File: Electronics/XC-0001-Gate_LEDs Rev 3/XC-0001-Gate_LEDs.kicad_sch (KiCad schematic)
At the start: 21 parts, among them J1 DC12V_IN, J2 Driver_Ext, J3 LED_DIM, J4 LED_NODIM, J5 AC_IN, J6 AC_OUT, J7 Dim_Select, U1 LDU1416S1000

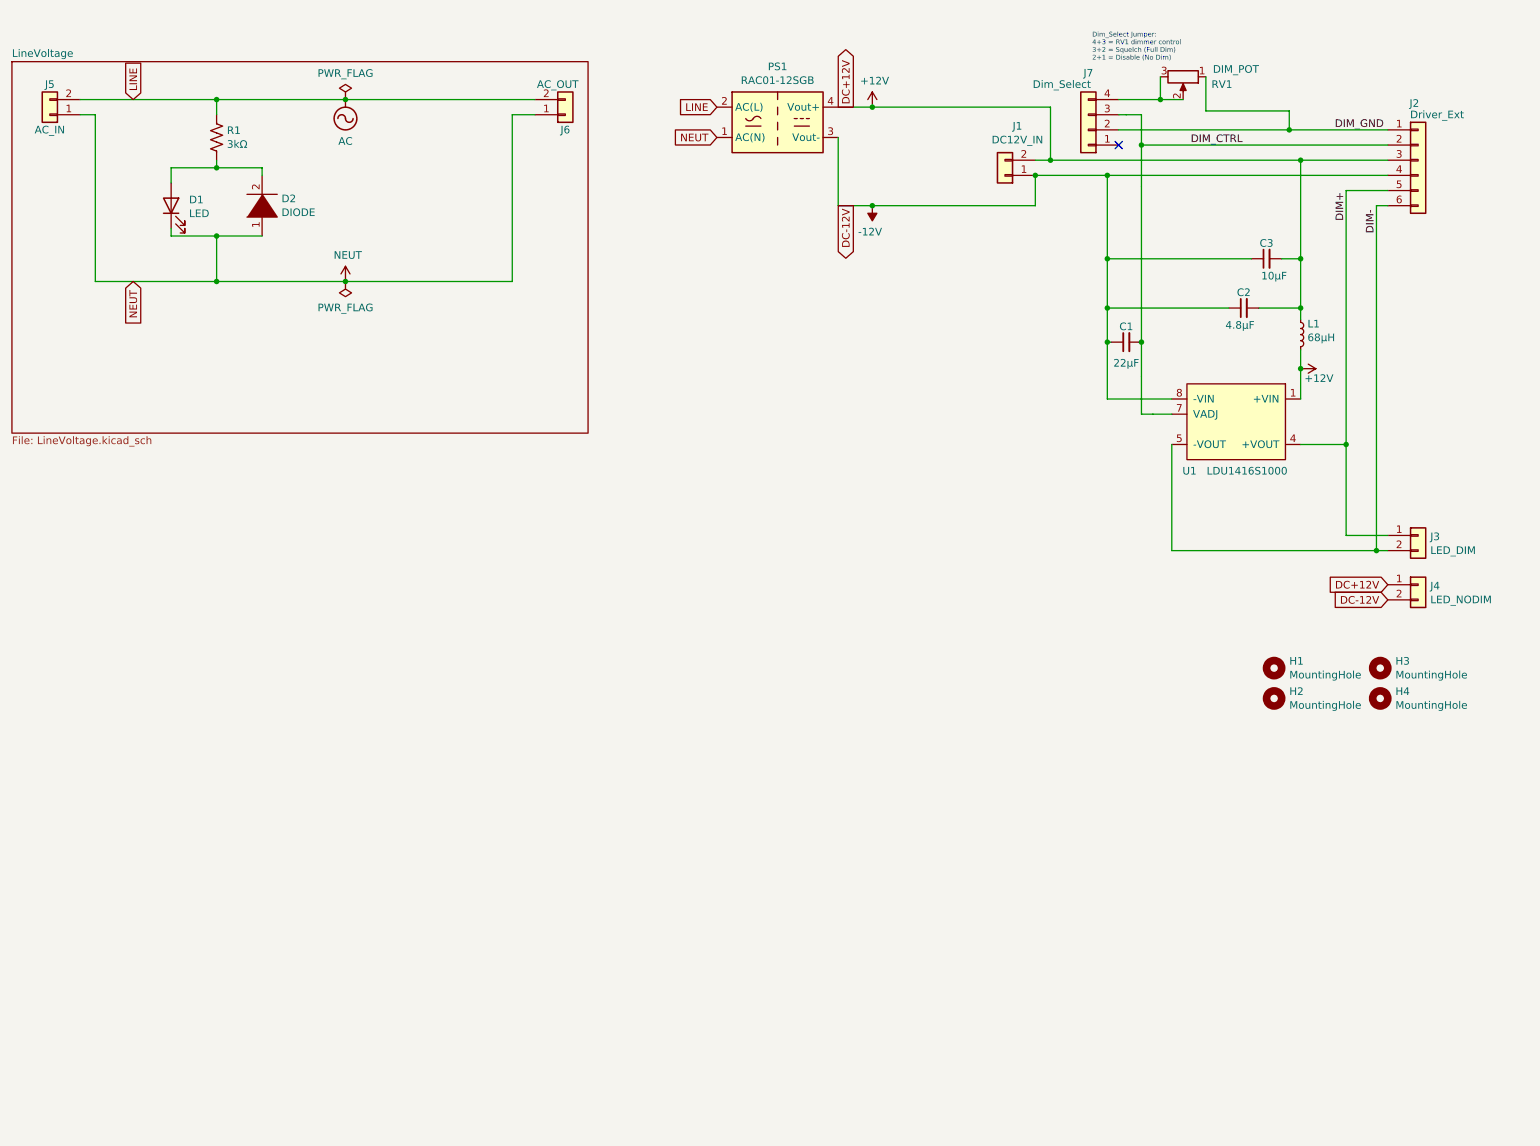
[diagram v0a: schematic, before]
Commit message: Ignore backup
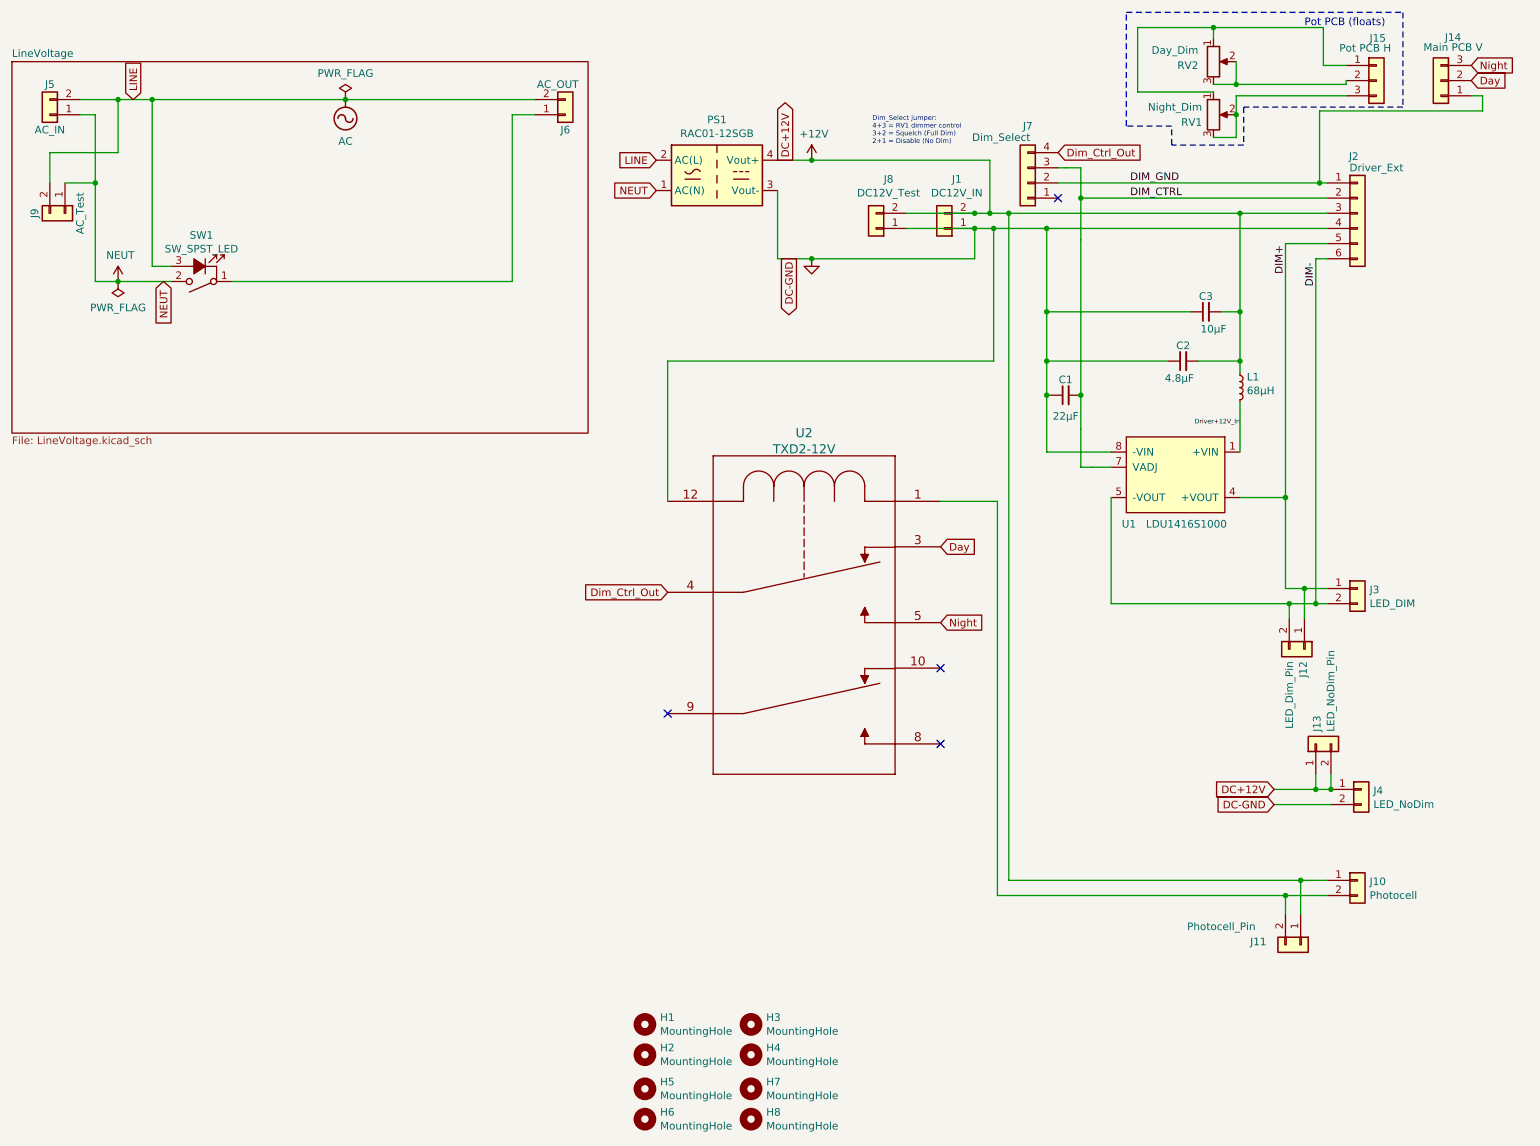
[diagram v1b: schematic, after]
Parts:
- removed D1: LED, Connector_Wire:SolderWire-0.5sqmm_1x02_P4.8mm_D0.9mm_OD2.3mm, symbol Device:LED
- removed D2: DIODE, Diode_THT:D_T-1_P10.16mm_Horizontal, symbol pspice:DIODE
- removed R1: 3kΩ, Resistor_SMD:R_1210_3225Metric_Pad1.30x2.65mm_HandSolder, symbol Device:R_US
- added H5, H6, H7, H8: MountingHole, MountingHole:MountingHole_3.2mm_M3, symbol Mechanical:MountingHole
- added J10: Photocell, Connector_Phoenix_MSTB:PhoenixContact_MSTBA_2,5_2-G-5,08_1x02_P5.08mm_Horizontal, symbol Connector_Generic:Conn_01x02
- added J11: Photocell_Pin, Connector_PinHeader_2.54mm:PinHeader_1x02_P2.54mm_Vertical, symbol Connector_Generic:Conn_01x02
- added J12: LED_Dim_Pin, Connector_PinHeader_2.54mm:PinHeader_1x02_P2.54mm_Vertical, symbol Connector_Generic:Conn_01x02
- added J13: LED_NoDim_Pin, Connector_PinHeader_2.54mm:PinHeader_1x02_P2.54mm_Vertical, symbol Connector_Generic:Conn_01x02
- added J14: Main PCB V, Connector_PinHeader_2.54mm:PinHeader_1x03_P2.54mm_Vertical, symbol Connector_Generic:Conn_01x03
- added J15: Pot PCB H, Connector_PinHeader_2.54mm:PinHeader_1x03_P2.54mm_Vertical, symbol Connector_Generic:Conn_01x03
- added J8: DC12V_Test, XC-footprint-lib:Test Holes, symbol Connector_Generic:Conn_01x02
- added J9: AC_Test, XC-footprint-lib:Test Holes, symbol Connector_Generic:Conn_01x02
- added RV2: Day_Dim, Potentiometer_THT:Potentiometer_Piher_PC-16_Single_Horizontal, symbol Device:R_POT
- added SW1: SW_SPST_LED, Connector_Phoenix_MSTB:PhoenixContact_MSTBVA_2,5_3-G-5,08_1x03_P5.08mm_Vertical, symbol XC-symbol-lib:SW_SPST_LED-Amazon_3_pole
- added U2: TXD2-12V, XC-footprint-lib:TXD2-12V, symbol XC-symbol-lib:TXD2-12V
- H1, H2, H3, H4: footprint MountingHole:MountingHole_3.2mm_M3_DIN965_Pad_TopOnly -> MountingHole:MountingHole_3.2mm_M3
- J3: footprint Connector_Wire:SolderWire-1.5sqmm_1x02_P7.8mm_D1.7mm_OD3.9mm -> Connector_Phoenix_MSTB:PhoenixContact_MSTBA_2,5_2-G-5,08_1x02_P5.08mm_Horizontal
- J4: value LED_NODIM -> LED_NoDim; footprint Connector_Wire:SolderWire-1.5sqmm_1x02_P7.8mm_D1.7mm_OD3.9mm -> Connector_Phoenix_MSTB:PhoenixContact_MSTBA_2,5_2-G-5,08_1x02_P5.08mm_Horizontal
- J5: footprint Connector_Wire:SolderWire-1.5sqmm_1x02_P7.8mm_D1.7mm_OD3.9mm -> XC-footprint-lib:6160.0015 C8 Inlet (panel mount, PCB pins)
- J6: footprint Connector_Wire:SolderWire-1.5sqmm_1x02_P7.8mm_D1.7mm_OD3.9mm -> Connector_Wire:SolderWire-2sqmm_1x02_P7.8mm_D2mm_OD3.9mm_Relief
- RV1: value DIM_POT -> Night_Dim
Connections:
- net +12V: now also J10.1 (Pin_1), J11.1 (Pin_1), J13.1 (Pin_1), J13.2 (Pin_2), J8.2 (Pin_2); no longer L1.2, U1.1 (+VIN)
- net AC: now also J9.2 (Pin_2), SW1.3 (Line_In)
- net DIM+: now also J12.1 (Pin_1)
- net DIM-: now also J12.2 (Pin_2)
- net DIM_GND: now also J14.1 (Pin_1); no longer RV1.1
- net NEUT: now also J9.1 (Pin_1), SW1.2 (Neutral_In); no longer J6.1 (Pin_1)
- net at RV1.2, RV1.3: now also J15.3 (Pin_3); no longer J7.4 (Pin_4)
- net -12V renamed GND
- net GND: now also J8.1 (Pin_1), U2.12
- new net: J15.1 (Pin_1), RV1.1, RV2.1
- new net: J6.1 (Pin_1), SW1.1 (Neutral_Out)
- new net: J10.2 (Pin_2), J11.2 (Pin_2), U2.1
- new net: J15.2 (Pin_2), RV2.2, RV2.3
- new net Day: J14.2 (Pin_2), U2.3
- new net Dim_Ctrl_Out: J7.4 (Pin_4), U2.4
- new net Driver+12V_In: L1.2, U1.1 (+VIN)
- new net Night: J14.3 (Pin_3), U2.5
- no-connect marks 1 -> 4
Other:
- note added: "Pot PCB (floats)"
- moved on the sheet: C1, C2, C3, H1, H2, H3, H4, J1, J2, J3, J4, J7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

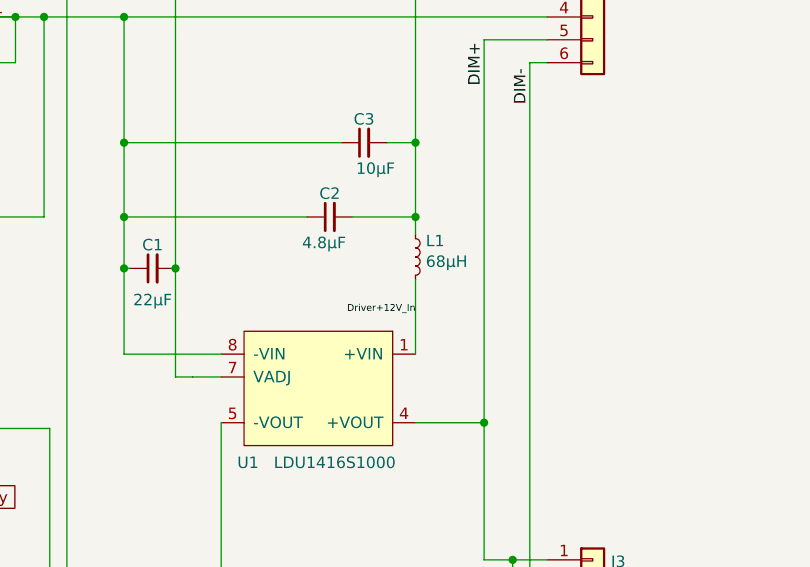
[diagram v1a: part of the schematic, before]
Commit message: Remove inductor to debug false pin connection
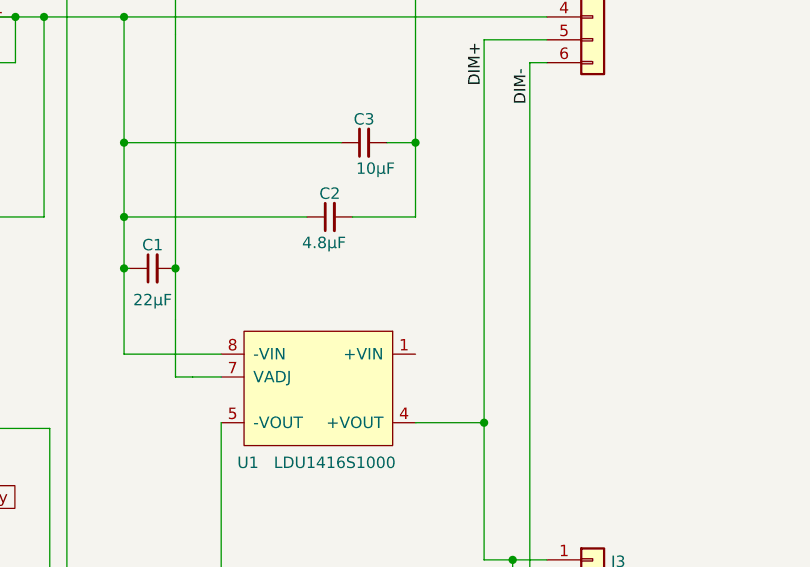
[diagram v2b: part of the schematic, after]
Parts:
- removed L1: 68µH, Inductor_THT:L_Radial_D9.5mm_P5.00mm_Fastron_07HVP, symbol Device:L_Small
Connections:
- net Driver+12V_In: no longer names the net of U1.1 (+VIN)
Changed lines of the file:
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@@
   (junction (at 220.98 46.99) (diameter 0.9144) (color 0 0 0 0))
   (junction (at 220.98 63.5) (diameter 0.9144) (color 0 0 0 0))
-  (junction (at 220.98 71.755) (diameter 0.9144) (color 0 0 0 0))
   (junction (at 228.6 94.615) (diameter 0.9144) (color 0 0 0 0))
   (junction (at 228.6 161.29) (diameter 0.9144) (color 0 0 0 0))
@@
     (stroke (width 0) (type solid) (color 0 0 0 0))
   )
-  (wire (pts (xy 220.98 71.755) (xy 220.98 73.66))
-    (stroke (width 0) (type solid) (color 0 0 0 0))
-  )
-  (wire (pts (xy 220.98 78.74) (xy 220.98 86.995))
-    (stroke (width 0) (type solid) (color 0 0 0 0))
-  )
   (wire (pts (xy 220.98 94.615) (xy 228.6 94.615))
     (stroke (width 0) (type solid) (color 0 0 0 0))
@@
   (label "DIM_CTRL" (at 202.565 44.45 0)
     (effects (font (size 1.27 1.27)) (justify left bottom))
-  )
-  (label "Driver+12V_In" (at 220.98 82.55 180)
-    (effects (font (size 0.76 0.76)) (justify right bottom))
   )
   (label "DIM+" (at 228.6 57.15 90)
@@
     )
     (pin "1")
-  )
-  (symbol (lib_id "Device:L_Small") (at 220.98 76.2 0) (unit 1)
-    (in_bom yes) (on_board yes)
-    (property "Reference" "L1" (id 0) (at 222.1231 74.4156 0)
-      (effects (font (size 1.27 1.27)) (justify left))
-    )
-    (property "Value" "68µH" (id 1) (at 222.123 76.714 0)
-      (effects (font (size 1.27 1.27)) (justify left))
-    )
-    (property "Footprint" "Inductor_THT:L_Radial_D9.5mm_P5.00mm_Fastron_07HVP" (id 2) (at 220.98 76.2 0)
-      (effects (font (size 1.27 1.27)) hide)
-    )
-    (property "Datasheet" "https://www.murata-ps.com/pub/data/magnetics/kmp_1300r.pdf" (id 3) (at 220.98 76.2 0)
-      (effects (font (size 1.27 1.27)) hide)
-    )
-    (property "Digikey" "811-2063-ND" (id 4) (at 220.98 76.2 0)
-      (effects (font (size 1.27 1.27)) hide)
-    )
-    (pin "1")
-    (pin "2")
   )
   (symbol (lib_id "power:PWR_FLAG") (at 33.02 58.42 180) (unit 1)
@@
       (reference "J15") (unit 1) (value "Pot PCB H") (footprint "Connector_PinHeader_2.54mm:PinHeader_1x03_P2.54mm_Vertical")
     )
-    (path "/4798a57e-a77e-44b7-a759-d2b71f4fd1ce"
-      (reference "L1") (unit 1) (value "68µH") (footprint "Inductor_THT:L_Radial_D9.5mm_P5.00mm_Fastron_07HVP")
-    )
     (path "/00000000-0000-0000-0000-000060332b0e"
